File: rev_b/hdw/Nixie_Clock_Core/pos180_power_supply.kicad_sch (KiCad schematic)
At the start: 36 parts

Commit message: more carrier board progress
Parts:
- removed C?: 10nF, Capacitors_SMD:C_0402, symbol Custom_Library:C_Custom
- removed R?: 22k, Resistors_SMD:R_0402, symbol Nixie-Clock-rescue:R
- added C?: 0.1uF, Capacitors_SMD:C_0603, symbol Custom_Library:C_Custom
- added R?: 100k, Resistors_SMD:R_0603, symbol Custom_Library:R_Custom
- R?: value 0.16 -> 0.36; Digi-Key PN (none) -> RL12S.36FCT-ND
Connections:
- net GND: now also C?.2
- net at U?.1 (VC): now also R?.1
- net at U?.3 (SS): now also C?.1
- net at C?.1: now also R?.2
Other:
- note added: "POS90_PGOOD COMPARATOR RESISTOR VALUES WRONG"
- note removed: "VERIFY COMPARATOR RESISTOR VALUES"
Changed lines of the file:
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@@
     (stroke (width 0) (type default))
   )
-  (text "VERIFY COMPARATOR RESISTOR VALUES" (at 59.69 143.51 0)
+  (text "POS90_PGOOD COMPARATOR RESISTOR VALUES WRONG" (at 59.69 143.51 0)
     (effects (font (face "Courier New") (size 5.08 5.08) (thickness 0.254) bold (color 255 37 56 1)) (justify left bottom))
   )
@@
       (effects (font (size 1.27 1.27)))
     )
-    (property "Value" "0.16" (at 134.62 96.52 90)
+    (property "Value" "0.36" (at 134.62 96.52 90)
       (effects (font (size 1.27 1.27)))
     )
@@
     (property "Footprint Display" "0805" (at 132.08 93.98 0)
       (effects (font (size 1.27 1.27)) (justify right))
+    )
+    (property "Digi-Key PN" "RL12S.36FCT-ND" (at 134.62 96.52 90)
+      (effects (font (size 1.27 1.27)) hide)
     )
     (pin "1")
@@
     )
   )
-  (symbol (lib_id "Custom_Library:C_Custom") (at 62.23 101.6 0) (unit 1)
-    (in_bom yes) (on_board yes) (dnp no)
-    (property "Reference" "C?" (at 62.865 99.06 0)
-      (effects (font (size 1.27 1.27)) (justify left))
-    )
-    (property "Value" "10nF" (at 62.865 104.14 0)
-      (effects (font (size 1.27 1.27)) (justify left))
-    )
-    (property "Footprint" "Capacitors_SMD:C_0402" (at 63.1952 105.41 0)
-      (effects (font (size 1.27 1.27)) hide)
-    )
-    (property "Datasheet" "" (at 62.865 99.06 0)
-      (effects (font (size 1.27 1.27)) hide)
-    )
-    (property "display_footprint" "0402" (at 58.42 99.06 0)
-      (effects (font (size 1.27 1.27)) (justify right))
-    )
-    (property "Voltage" "50V" (at 58.42 101.6 0)
-      (effects (font (size 1.27 1.27)) (justify right))
-    )
-    (property "Dielectric" "X7R" (at 58.42 104.14 0)
-      (effects (font (size 1.27 1.27)) (justify right))
-    )
-    (property "Digi-Key PN" "399-3066-1-ND" (at 73.025 88.9 0)
-      (effects (font (size 1.524 1.524)) hide)
-    )
-    (pin "1")
-    (pin "2")
-    (instances
-      (project "Nixie_Clock_Core"
-        (path "/16fdce21-b570-4d81-a458-e8839d611806/0b6dccc1-0a92-424d-9916-2441ea7dc052"
-          (reference "C?") (unit 1)
-        )
-        (path "/16fdce21-b570-4d81-a458-e8839d611806/033277b9-3b61-4d88-889d-97b223ca74c5"
-          (reference "C?") (unit 1)
-        )
-        (path "/16fdce21-b570-4d81-a458-e8839d611806/b9e3b07e-337a-481e-964b-cf3238d1c75e"
-          (reference "C?") (unit 1)
-        )
-      )
-      (project "LED_Panel_Controller"
-        (path "/22e05ee1-b227-4be7-9418-94433f274720/00000000-0000-0000-0000-00005bb181d8"
-          (reference "C?") (unit 1)
-        )
-        (path "/22e05ee1-b227-4be7-9418-94433f274720/00000000-0000-0000-0000-00005baae0fa"
-          (reference "C?") (unit 1)
-        )
-        (path "/22e05ee1-b227-4be7-9418-94433f274720/00000000-0000-0000-0000-00005d77a516"
-          (reference "C?") (unit 1)
-        )
-        (path "/22e05ee1-b227-4be7-9418-94433f274720/00000000-0000-0000-0000-00005eae2d66"
-          (reference "C?") (unit 1)
-        )
-        (path "/22e05ee1-b227-4be7-9418-94433f274720/00000000-0000-0000-0000-00005baae16c"
-          (reference "C?") (unit 1)
-        )
-        (path "/22e05ee1-b227-4be7-9418-94433f274720/00000000-0000-0000-0000-00005bb86f23"
-          (reference "C?") (unit 1)
-        )
-        (path "/22e05ee1-b227-4be7-9418-94433f274720/00000000-0000-0000-0000-00005f581b41"
-          (reference "C?") (unit 1)
-        )
-        (path "/22e05ee1-b227-4be7-9418-94433f274720/00000000-0000-0000-0000-00005e939cff"
-          (reference "C?") (unit 1)
-        )
-        (path "/22e05ee1-b227-4be7-9418-94433f274720/00000000-0000-0000-0000-00005bb2595e"
-          (reference "C?") (unit 1)
-        )
-      )
-    )
-  )
   (symbol (lib_id "Nixie-Clock-rescue:R") (at 62.23 74.93 0) (unit 1)
     (in_bom yes) (on_board yes) (dnp no)
@@
         (path "/2a5e6550-1edc-4b7d-9ce1-3930249972d7/00000000-0000-0000-0000-000058b0f8c0"
           (reference "#PWR?") (unit 1)
+        )
+      )
+    )
+  )
+  (symbol (lib_id "Custom_Library:R_Custom") (at 88.9 118.11 0) (mirror y) (unit 1)
+    (in_bom yes) (on_board yes) (dnp no)
+    (property "Reference" "R?" (at 87.122 114.808 0)
+      (effects (font (size 1.27 1.27)) (justify left))
+    )
+    (property "Value" "100k" (at 88.9 118.11 90)
+      (effects (font (size 1.016 1.016)))
+    )
+    (property "Footprint" "Resistors_SMD:R_0603" (at 88.9 118.11 0)
+      (effects (font (size 1.27 1.27)) hide)
+    )
+    (property "Datasheet" "" (at 88.9 118.11 0)
+      (effects (font (size 1.27 1.27)) hide)
+    )
+    (property "display_footprint" "0603" (at 87.122 116.84 0)
+      (effects (font (size 1.27 1.27)) (justify left))
+    )
+    (property "Tolerance" "1%" (at 87.122 119.126 0)
+      (effects (font (size 1.27 1.27)) (justify left))
+    )
+    (property "Wattage" "1/10W" (at 87.122 121.412 0)
+      (effects (font (size 1.27 1.27)) (justify left))
+    )
+    (property "Digi-Key PN" "RMCF0603FT100KCT-ND" (at 88.9 118.11 0)
+      (effects (font (size 1.27 1.27)) hide)
+    )
+    (pin "1")
+    (pin "2")
+    (instances
+      (project "Analog_Clock"
+        (path "/0dc9b974-a945-4291-bc55-04b8e342b0e5/00000000-0000-0000-0000-00005e939f76"
+          (reference "R?") (unit 1)
+        )
+        (path "/0dc9b974-a945-4291-bc55-04b8e342b0e5/00000000-0000-0000-0000-00005e939d51"
+          (reference "R?") (unit 1)
+        )
+      )
+      (project "Nixie_Clock_Core"
+        (path "/16fdce21-b570-4d81-a458-e8839d611806/4cb440c2-4356-400c-9387-edaaa635d5a5"
+          (reference "R?") (unit 1)
+        )
+        (path "/16fdce21-b570-4d81-a458-e8839d611806/0b6dccc1-0a92-424d-9916-2441ea7dc052"
+          (reference "R?") (unit 1)
         )
       )
@@
     )
   )
-  (symbol (lib_id "Nixie-Clock-rescue:R") (at 88.9 118.11 0) (unit 1)
-    (in_bom yes) (on_board yes) (dnp no)
-    (property "Reference" "R?" (at 90.932 118.11 90)
-      (effects (font (size 1.27 1.27)))
-    )
-    (property "Value" "22k" (at 88.9 118.11 90)
-      (effects (font (size 1.27 1.27)))
-    )
-    (property "Footprint" "Resistors_SMD:R_0402" (at 82.55 115.57 0)
-      (effects (font (size 1.27 1.27)) (justify left) hide)
-    )
-    (property "Datasheet" "" (at 90.932 118.11 90)
-      (effects (font (size 1.27 1.27)))
-    )
-    (property "Wattage" "1/16W" (at 86.36 120.65 0)
-      (effects (font (size 1.27 1.27)) (justify right))
-    )
-    (property "Tolerance" "1%" (at 86.36 118.11 0)
-      (effects (font (size 1.27 1.27)) (justify right))
-    )
-    (property "Footprint Display" "0402" (at 86.36 115.57 0)
-      (effects (font (size 1.27 1.27)) (justify right))
-    )
-    (pin "1")
-    (pin "2")
-    (instances
-      (project "Nixie_Clock_Core"
-        (path "/16fdce21-b570-4d81-a458-e8839d611806/0b6dccc1-0a92-424d-9916-2441ea7dc052"
-          (reference "R?") (unit 1)
-        )
-      )
-      (project "Nixie Clock"
-        (path "/2a5e6550-1edc-4b7d-9ce1-3930249972d7/00000000-0000-0000-0000-000058b0f8c0"
-          (reference "R?") (unit 1)
-        )
-      )
-    )
-  )
   (symbol (lib_id "Custom_Library:C_Custom") (at 140.97 187.96 0) (mirror y) (unit 1)
     (in_bom yes) (on_board yes) (dnp no)
@@
         )
       )
+    )
+  )
+  (symbol (lib_id "Custom_Library:C_Custom") (at 62.23 101.6 0) (mirror y) (unit 1)
+    (in_bom yes) (on_board yes) (dnp no)
+    (property "Reference" "C?" (at 61.595 99.06 0)
+      (effects (font (size 1.27 1.27)) (justify left))
+    )
+    (property "Value" "0.1uF" (at 61.595 104.14 0)
+      (effects (font (size 1.27 1.27)) (justify left))
+    )
+    (property "Footprint" "Capacitors_SMD:C_0603" (at 61.2648 105.41 0)
+      (effects (font (size 1.27 1.27)) hide)
+    )
+    (property "Datasheet" "" (at 61.595 99.06 0)
+      (effects (font (size 1.27 1.27)) hide)
+    )
+    (property "Digi-Key PN" "399-7845-1-ND" (at 51.435 88.9 0)
+      (effects (font (size 1.524 1.524)) hide)
+    )
+    (property "display_footprint" "0603" (at 66.04 99.06 0)
+      (effects (font (size 1.27 1.27)) (justify right))
+    )
+    (property "Voltage" "50V" (at 66.04 101.6 0)
+      (effects (font (size 1.27 1.27)) (justify right))
+    )
+    (property "Dielectric" "X7R" (at 66.04 104.14 0)
+      (effects (font (size 1.27 1.27)) (justify right))
+    )
+    (pin "1")
+    (pin "2")
+    (instances
+      (project "Analog_Clock"
+        (path "/0dc9b974-a945-4291-bc55-04b8e342b0e5/00000000-0000-0000-0000-00005baae1cb"
+          (reference "C?") (unit 1)
+        )
+        (path "/0dc9b974-a945-4291-bc55-04b8e342b0e5/00000000-0000-0000-0000-00005cad2d97"
+          (reference "C?") (unit 1)
+        )
+        (path "/0dc9b974-a945-4291-bc55-04b8e342b0e5/00000000-0000-0000-0000-00005baae1f3"
+          (reference "C?") (unit 1)
+        )
+        (path "/0dc9b974-a945-4291-bc55-04b8e342b0e5/00000000-0000-0000-0000-00005e939f76"
+          (reference "C?") (unit 1)
+        )
+        (path "/0dc9b974-a945-4291-bc55-04b8e342b0e5/00000000-0000-0000-0000-00005be48f98"
+          (reference "C?") (unit 1)
+        )
+      )
+      (project "Nixie_Clock_Core"
+        (path "/16fdce21-b570-4d81-a458-e8839d611806/4cb440c2-4356-400c-9387-edaaa635d5a5"
+          (reference "C?") (unit 1)
+        )
+        (path "/16fdce21-b570-4d81-a458-e8839d611806/0b6dccc1-0a92-424d-9916-2441ea7dc052"
+          (reference "C?") (unit 1)
+        )
+      )

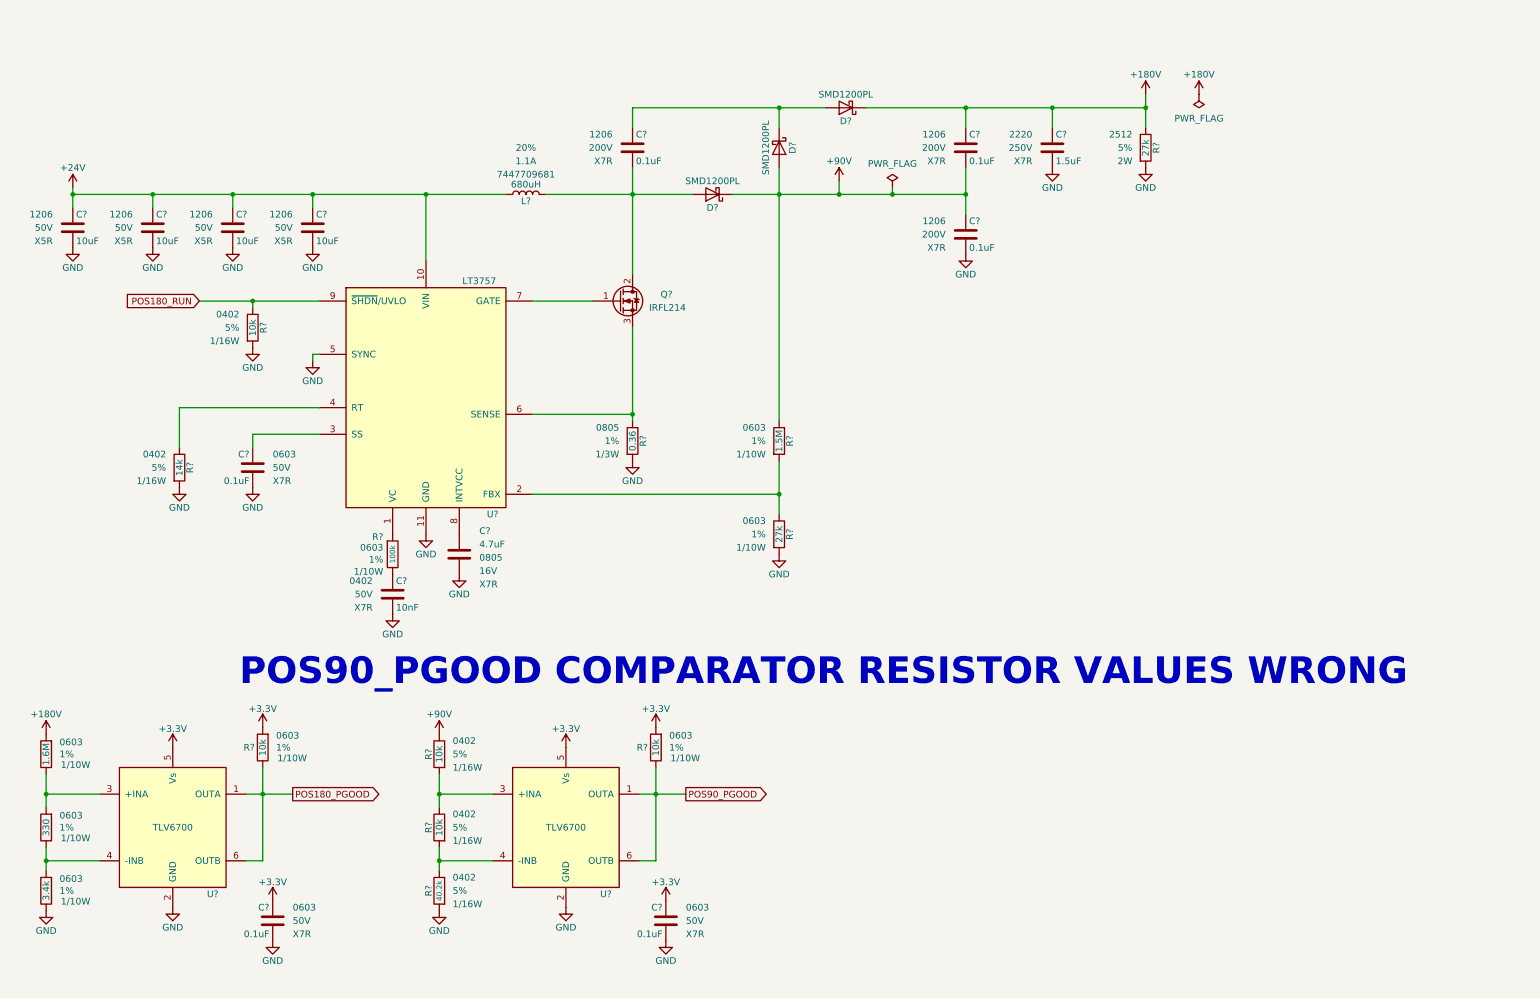
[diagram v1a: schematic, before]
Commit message: revamped POS180 telemetry
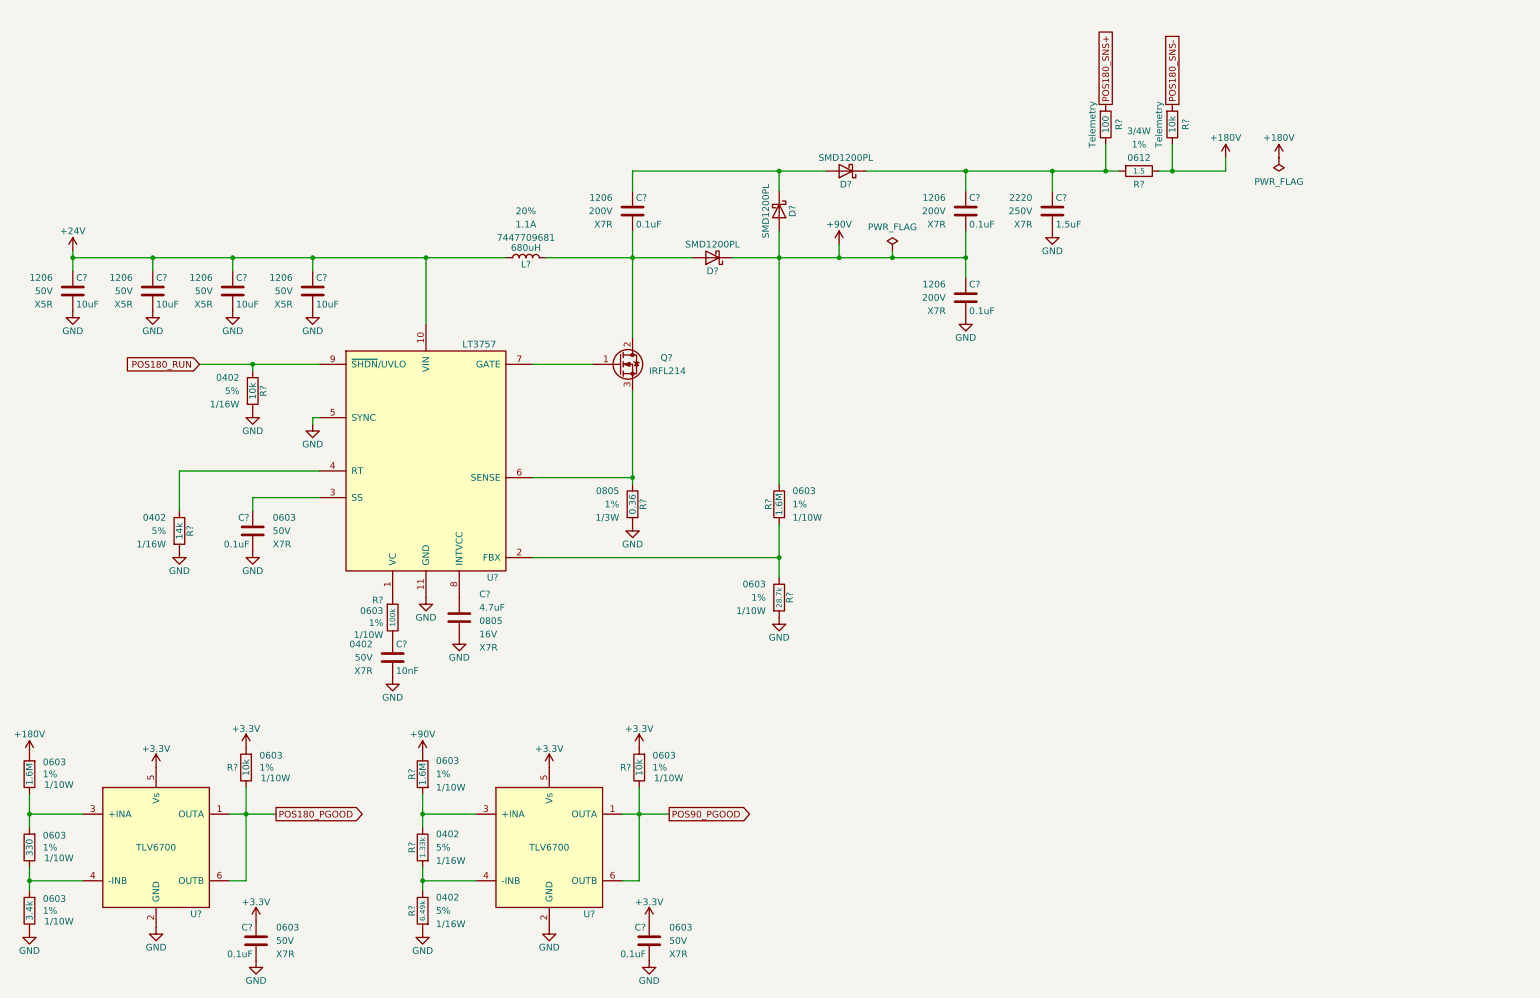
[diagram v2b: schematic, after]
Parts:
- removed R?: 1.5M, Resistors_SMD:R_0603, symbol Nixie-Clock-rescue:R
- removed R?: 10k, Resistors_SMD:R_0402, symbol Nixie-Clock-rescue:R
- removed R?: 27k, Resistors_SMD:R_2512, symbol Nixie-Clock-rescue:R
- added R?: 1.5, Resistors_SMD:R_0612, symbol Custom_Library:R_Custom
- added R? (x2): 1.6M, Resistors_SMD:R_0603, symbol Nixie-Clock-rescue:R
- added R?: 100, Resistors_SMD:R_0402, symbol Custom_Library:R_Custom
- added R?: 10k, Resistors_SMD:R_0402, symbol Custom_Library:R_Custom
- R?: value 10k -> 1.33k
- R?: value 40.2k -> 6.49k
- R?: value 27k -> 28.7k
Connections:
- net +180V: now also R?.1, R?.1, R?.2, R?.2; no longer C?.1, C?.1, D?.1 (K)
- net at R?.1, U?.2 (FBX): now also R?.2
- net at R?.1, U?.3 (+INA): now also R?.2
- new net: C?.1, C?.1, D?.1 (K), R?.1, R?.2
- new net POS180_SNS+: R?.1
- new net POS180_SNS-: R?.1
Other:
- note removed: "POS90_PGOOD COMPARATOR RESISTOR VALUES WRONG"
- moved on the sheet: C?, D?, L?, Q?, R?, U?

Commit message: updated footprints, ran some DRC
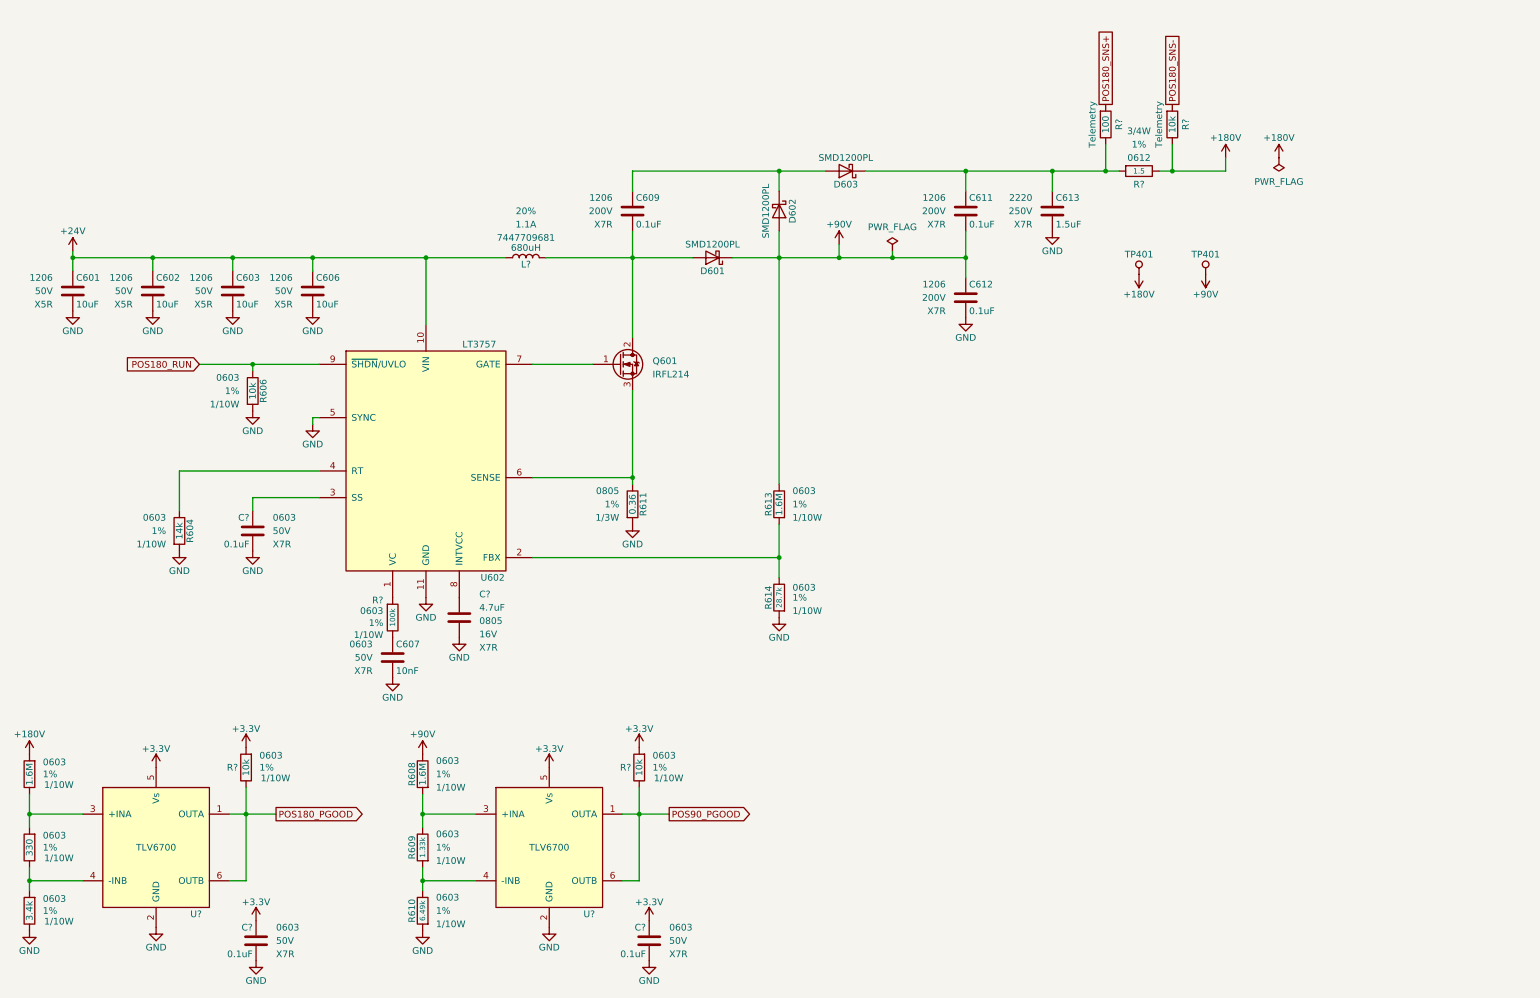
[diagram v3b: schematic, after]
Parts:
- added TP401 (x2): TP, Custom Footprints Library:Test_Point, symbol Custom_Library:TP
- C601, C602, C603, C606: renamed from C?; footprint (none) -> Capacitors_SMD:C_1206; Digi-Key PN 1276-6736-1-ND -> (none)
- C607: renamed from C?; footprint Capacitors_SMD:C_0402 -> Capacitors_SMD:C_0603; Digi-Key PN 399-3066-1-ND -> (none); display_footprint 0402 -> 0603
- C609, C611, C612: renamed from C?; footprint (none) -> Capacitors_SMD:C_1206; Digi-Key PN 399-C1206J104K2RACAUTOCT-ND -> (none)
- C613: renamed from C?; footprint (none) -> Capacitors_SMD:C_2220; Digi-Key PN 565-4697-1-ND -> (none)
- C? (x3): Digi-Key PN 399-7845-1-ND -> (none)
- C?: Digi-Key PN 1276-2970-1-ND -> (none)
- D601, D602, D603: renamed from D?; Footprint Display SOD-123F -> (none); display_footprint (none) -> SOD-123F
- Q601: renamed from Q?; footprint Custom Footprints:SOT-223_3 -> Package_TO_SOT_SMD:SOT-223-3_TabPin2
- R604, R606, R609: renamed from R?; footprint Resistors_SMD:R_0402 -> Resistors_SMD:R_0603; Footprint Display 0402 -> (none); Tolerance 5% -> 1%; Wattage 1/16W -> 1/10W; display_footprint (none) -> 0603
- R608, R613, R614: renamed from R?; Footprint Display 0603 -> (none); display_footprint (none) -> 0603
- R610: renamed from R?; Footprint Display 0402 -> (none); Tolerance 5% -> 1%; Wattage 1/16W -> 1/10W; display_footprint (none) -> 0603
- R611: renamed from R?; Footprint Display 0805 -> (none); display_footprint (none) -> 0805
- R?: Digi-Key PN RMCF0603FT100KCT-ND -> (none)
- R? (x2): Digi-Key PN YAG2321CT-ND -> (none)
- R? (x2): footprint Resistors_SMD:R_0402 -> Resistors_SMD:R_0603; Wattage 1/16W -> 1/10W; display_footprint 0402 -> 0603
- gave numbers to parts that had none: 1
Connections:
- net +180V: now also TP401.1 (TP); no longer C611.2, C612.1, D601.1 (K), D602.2 (A), R613.1
- new net +90V: C611.2, C612.1, D601.1 (K), D602.2 (A), R613.1, TP401.1 (TP)
